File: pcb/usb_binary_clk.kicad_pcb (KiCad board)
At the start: 2 copper layers, 40 parts, among them J1 USB_B_Micro, J2 USB_B_Micro, SW1 SW_Push, SW2 SW_Push, SW3 SW_Push, U1 MCP7940N-xP, U2 ATtiny84V-10PU, Y1 Crystal

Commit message: Modify pcb layout
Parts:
- BT1, J1, J2: moved to B.Cu
- moved R3 145.9 mm to (129.5, 76.2)
- moved J1 133.2 mm to (142.2, 29.8)
- moved C1 125.8 mm to (152.4, 83.3), turned to 270 degrees
- moved J2 114.4 mm to (170.2, 27.9)
- moved R9 95.9 mm to (171.4, 51.4)
- moved R5 92.7 mm to (155.6, 89.5), turned to 90 degrees
- moved R10 89.3 mm to (158.8, 81.9), turned to 270 degrees
- moved R8 84.6 mm to (171.4, 62.9)
- moved C4 84.5 mm to (161.9, 88.3), turned to 90 degrees
- moved R6 74.8 mm to (171.4, 74.3)
- moved C3 41.0 mm to (167.6, 77.5), turned to 180 degrees
- moved C2 40.2 mm to (162.6, 74.9)
- moved D17 33.1 mm to (142.2, 76.2)
- moved Y1 12.8 mm to (160.0, 74.9)
- moved U1 12.7 mm to (174.0, 82.5), turned to 270 degrees
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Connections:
- U1 pad 5: /scl -> /sda
- U1 pad 6: /sda -> /scl
- Y1 pad 1: /clk- -> /clk+
- Y1 pad 2: /clk+ -> /clk-
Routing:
- net /clk+: track 8.67 -> 0.11 mm
- net /clk-: track 5.08 -> 0.00 mm
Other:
- board outline added: 55.9 x 77.5 mm

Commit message: fix pcb design
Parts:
- added G***: LOGO, LOGO, F.Cu at (153.5, 8.17)
- added G***: LOGO, LOGO, F.Cu at (154.7, 62.8)
- moved C3 11.4 mm to (167.6, 88.9)
- moved D13 11.4 mm to (142.2, 80.0)
- moved D14 11.4 mm to (149.9, 80.0)
- moved D15 11.4 mm to (157.5, 80.0)
- moved D16 11.4 mm to (165.1, 80.0)
- moved R5 11.4 mm to (155.6, 101.0)
- moved R7 11.4 mm to (129.5, 80.0)
- moved SW1 11.4 mm to (175.3, 80.0)
- moved U1 11.4 mm to (174.0, 94.0)
- moved D1 11.4 mm to (142.2, 57.1)
- moved D10 11.4 mm to (149.9, 72.4)
- moved D11 11.4 mm to (157.5, 72.4)
- moved D12 11.4 mm to (165.1, 72.4)
- moved D2 11.4 mm to (149.9, 57.1)
- moved D3 11.4 mm to (157.5, 57.1)
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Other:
- board size 55.9 x 77.5 mm -> 55.6 x 83.8 mm

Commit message: fix pcb design (for real this time)
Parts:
- removed the G*** at (153.5, 8.17)
- removed the G*** at (154.7, 62.8)
- added G***: LOGO, LOGO, F.Cu at (154.1, 69.2)
- moved BT1 101.0 mm to (153.0, 126.4)
- moved J1 101.0 mm to (140.3, 130.8)
- moved J2 101.0 mm to (168.3, 128.9)

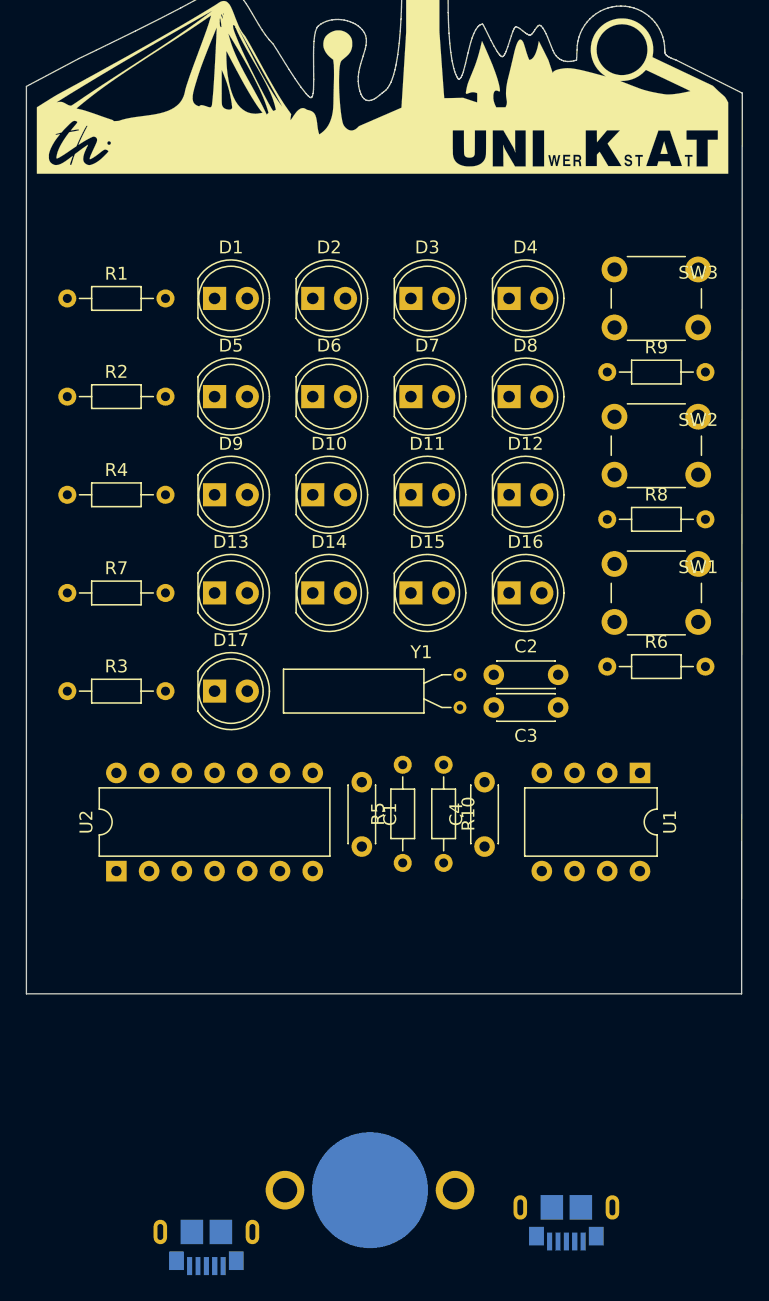
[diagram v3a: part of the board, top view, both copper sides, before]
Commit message: finalizes part position
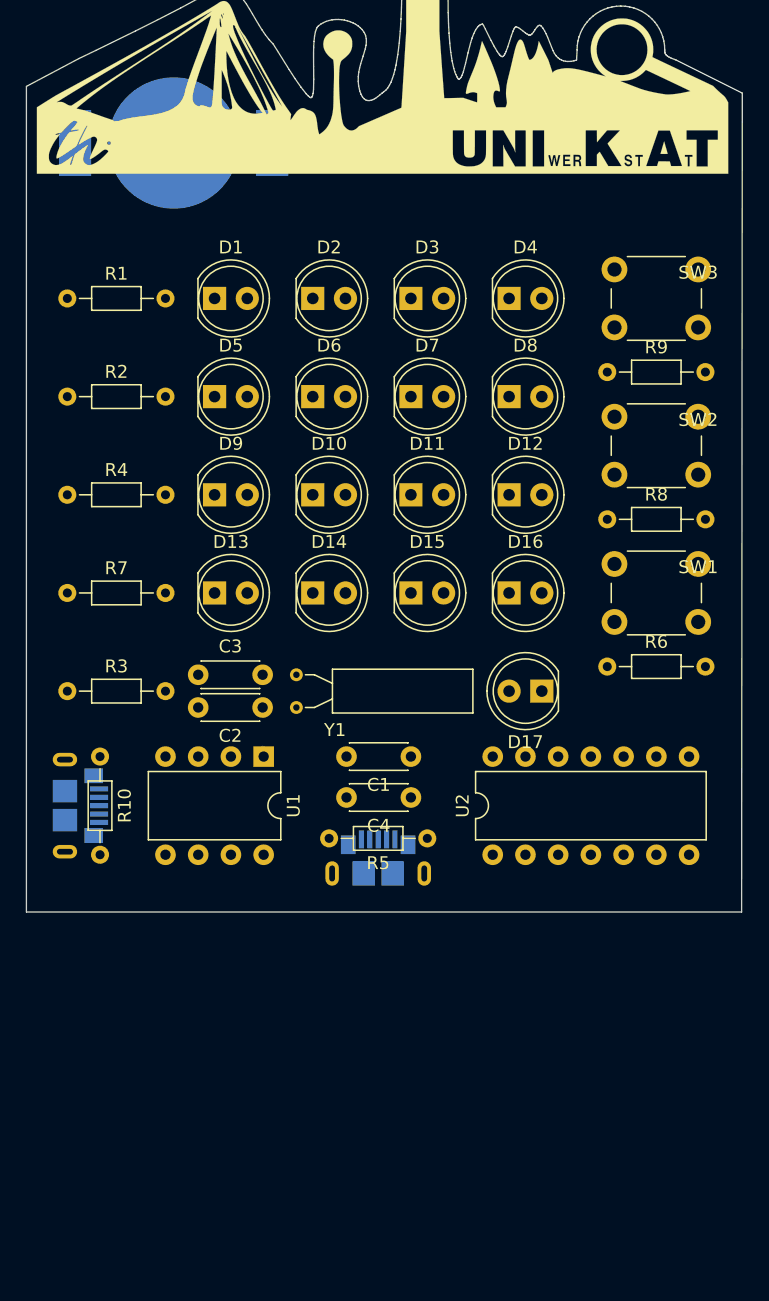
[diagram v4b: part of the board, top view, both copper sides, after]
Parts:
- BT1: footprint Battery:BatteryHolder_Keystone_3001_1x12mm -> binary_clk_parts:bat-hld-012
- moved BT1 82.7 mm to (137.8, 45.1)
- moved J1 35.7 mm to (130.6, 96.5), turned to 90 degrees
- moved J2 31.9 mm to (153.7, 100.6), turned to 180 degrees
- moved U1 29.2 mm to (144.8, 92.7)
- moved U2 29.2 mm to (162.6, 100.3)
- moved C3 28.1 mm to (139.7, 86.4), turned to 0 degrees
- moved R10 26.7 mm to (132.1, 92.7)
- moved D17 22.9 mm to (165.1, 87.6), turned to 180 degrees
- moved C2 18.1 mm to (144.7, 88.9), turned to 180 degrees
- moved Y1 13.0 mm to (147.3, 88.9), turned to 90 degrees
- moved C4 6.87 mm to (156.2, 95.9), turned to 180 degrees
- moved C1 4.30 mm to (156.2, 92.7), turned to 180 degrees
- moved R5 2.69 mm to (157.5, 99.1), turned to 180 degrees
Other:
- board size 55.6 x 83.8 mm -> 55.6 x 77.4 mm

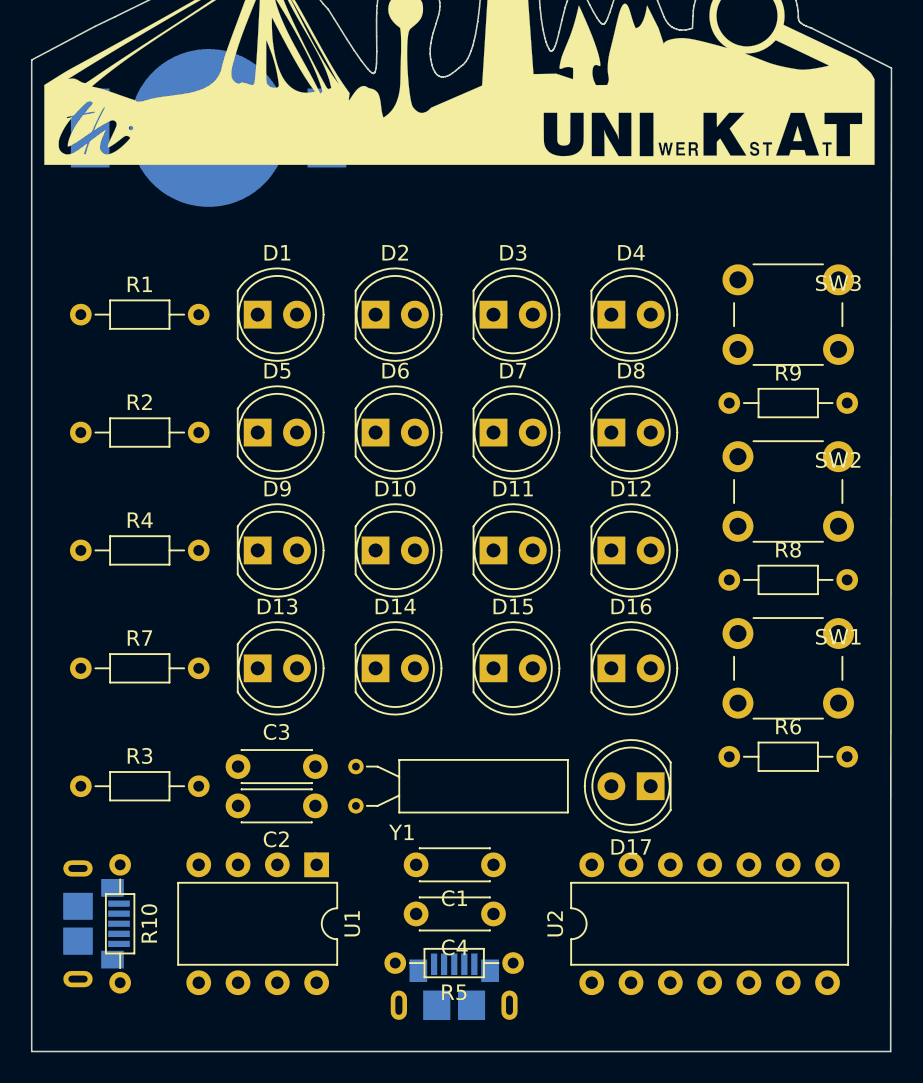
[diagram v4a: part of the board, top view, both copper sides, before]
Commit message: change usb port footprints, add programmer pads
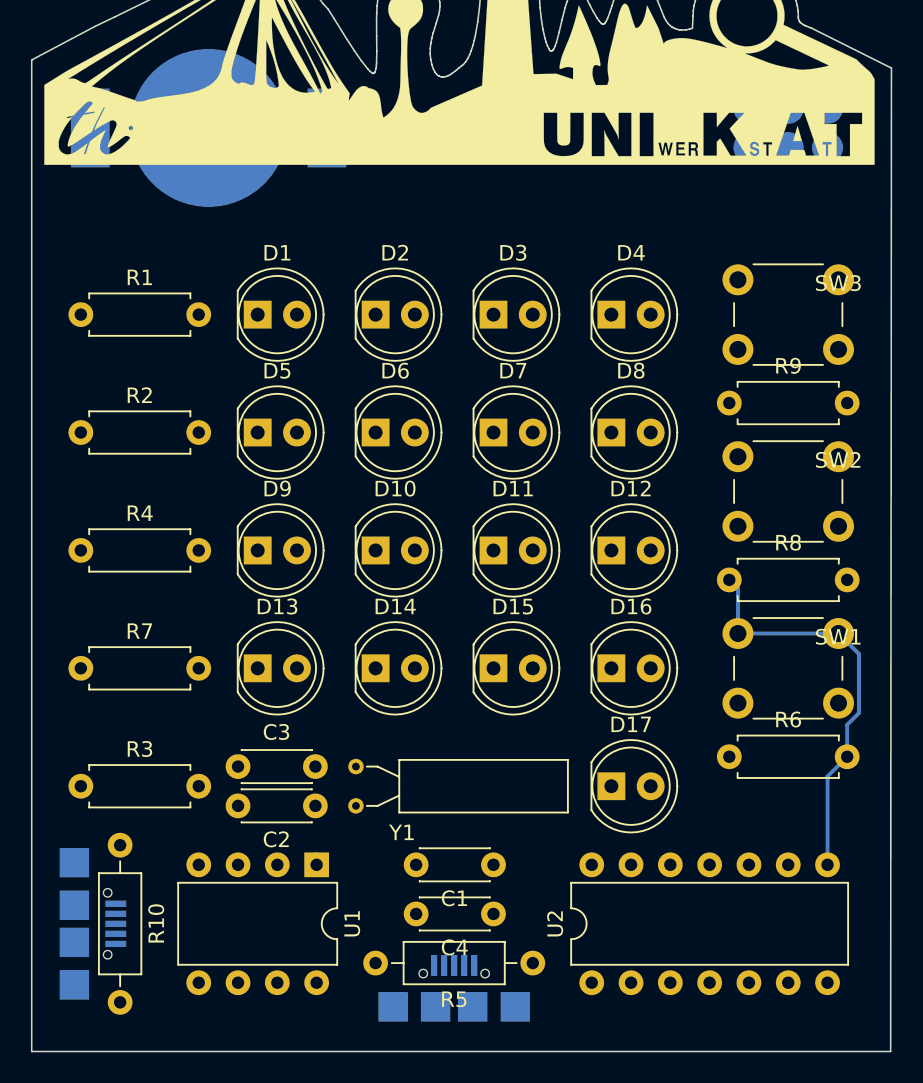
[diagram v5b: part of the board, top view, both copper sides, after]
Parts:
- added J3: AVR-ISP-6, binary_clk_parts:isp_pogoPinPads, B.Cu at (175.3, 45.1)
- J1, J2: footprint Connector_USB:USB_Micro-B_GCT_USB3076-30-A -> binary_clk_parts:UJ2MIBHGSMTTR
- R1, R2, R3, R4, R6, R7, R8, R9: footprint Resistor_THT:R_Axial_DIN0204_L3.6mm_D1.6mm_P7.62mm_Horizontal -> Resistor_THT:R_Axial_DIN0207_L6.3mm_D2.5mm_P7.62mm_Horizontal
- R10, R5: footprint Resistor_THT:R_Axial_DIN0204_L3.6mm_D1.6mm_P7.62mm_Horizontal -> Resistor_THT:R_Axial_DIN0207_L6.3mm_D2.5mm_P10.16mm_Horizontal
- moved J1 1.40 mm to (129.2, 96.5)
- moved R5 1.27 mm to (158.8, 99.1)
- moved J2 1.27 mm to (153.7, 101.9)
- moved R10 1.27 mm to (132.1, 91.4)
- turned D17 to 0 degrees
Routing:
- net /sw: track 0.00 -> 26.5 mm

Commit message: add routing
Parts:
- moved C2 0.25 mm to (144.7, 89.2)
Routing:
- net /col01: track 0.00 -> 83.0 mm
- net /col23: track 0.00 -> 78.6 mm
- net /row0: track 0.00 -> 69.6 mm
- net /row1: track 0.00 -> 59.8 mm
- net /row2: track 0.00 -> 50.0 mm
- net /row3: track 0.00 -> 40.8 mm
- net Net-(D10-Pad1): track 0.00 -> 28.7 mm
- net Net-(D13-Pad2): track 0.00 -> 28.7 mm
- net Net-(D5-Pad2): track 0.00 -> 28.7 mm
- net Net-(D1-Pad2): track 0.00 -> 28.7 mm
- net Net-(R8-Pad2): track 0.00 -> 18.7 mm
- net /clk+: track 0.00 -> 15.5 mm
- net Net-(R9-Pad2): track 0.00 -> 15.0 mm
- net /clk-: track 0.11 -> 14.1 mm
- net GND: track 0.00 -> 12.5 mm
- added copper zone on B.Cu, net GND
- added copper zone on F.Cu, net GND

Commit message: add routing (forgot to save last time)
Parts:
- moved R10 27.7 mm to (158.8, 99.1), turned to 180 degrees
- moved R5 26.8 mm to (132.1, 101.6), turned to 90 degrees
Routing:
- net +5V: track 0.00 -> 81.4 mm, vias 0 -> 2
- net +BATT: track 0.00 -> 77.2 mm, vias 0 -> 1
- net /scl: track 0.00 -> 55.9 mm
- net /sda: track 0.00 -> 47.3 mm
- net /photodiode: track 0.00 -> 35.3 mm
- net GND: track 12.5 -> 18.3 mm

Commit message: tune crystal paths, add vias
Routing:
- net /clk+: track 15.5 -> 17.2 mm
- net /clk-: track 14.1 -> 14.6 mm
- net GND: vias 0 -> 12
